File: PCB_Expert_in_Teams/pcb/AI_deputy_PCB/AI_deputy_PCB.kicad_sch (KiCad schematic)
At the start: 23 parts, among them J1 Piezo Electric, J3 Haptic Power and GND, J4 UART, J5 JST CONN from MCU, J6 JTAG, Q1 NMOS, SW1 BOOT SWITCH, SW2 RESET SWITCH, U2 ESP32-WROOM-32UE

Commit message: updating repo from desktop
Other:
- note added: "Keep as close to MCU pins as possible"
- note removed: "Keep close to MCU pins as possible"
- moved on the sheet: C1, C3, J1, J4, L1, Q1, R2, R3, R4, SW1A, SW2A

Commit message: progress on PCB + matlab calculations
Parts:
- added J15: Conn_01x04_Socket, symbol Connector:Conn_01x04_Socket
- J1: footprint Connector_JST:JST_XH_B1B-XH-AM_1x01_P2.50mm_Vertical -> Connector_JST:JST_XH_S2B-XH-A-1_1x02_P2.50mm_Horizontal
- Q1: footprint (none) -> Package_TO_SOT_SMD:TO-252-3_TabPin2
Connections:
- net +3V3: now also J15.2 (Pin_2)
- net GND: now also J15.1 (Pin_1)
- net Signal Left: now reaches U2.10 (IO25)
- net Signal Left: now also J15.3 (Pin_3)
- net Signal Right: now reaches U2.11 (IO26)
- net Signal Right: now also J15.4 (Pin_4)
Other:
- added sheet Stepdown3v3 (stepdown3v3.kicad_sch)
- added sheet stepup12v (stepup12v.kicad_sch)

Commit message: 29/10/update
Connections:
- net VDD is gone; now on net VDD33: C9.2
- net USB_TX: now reaches J4.3 (Pin_3), U2.34 (RXD0/IO3)
- net USB_RX: now reaches J4.2 (Pin_2), U2.35 (TXD0/IO1)
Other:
- sheet PD and UART renamed PD and USBC
- added sheet LI_Charge_IC (LI_Charge_IC.kicad_sch)
- added sheet UART (UART.kicad_sch)
- note added: "connect me"
- note added: "find fitting res value for led"
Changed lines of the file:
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@@
 	(title_block
 		(title "AI Deputy")
-		(date "2025-09-24")
+		(date "2025-10-29")
 		(rev "v0.1")
 		(company "Area 42 & Albers-Online Psykologi")
@@
 		)
 	)
+	(text "connect me\n"
+		(exclude_from_sim no)
+		(at 181.356 122.174 0)
+		(effects
+			(font
+				(size 1.27 1.27)
+			)
+		)
+	)
+	(text "find fitting res \nvalue for led\n"
+		(exclude_from_sim no)
+		(at 198.374 53.594 0)
+		(effects
+			(font
+				(size 1.27 1.27)
+			)
+		)
+	)
 	(text_box ""
 		(exclude_from_sim no)
@@
 		)
 	)
-	(global_label "VDD"
-		(shape input)
-		(at 161.29 60.96 270)
-		(fields_autoplaced yes)
-		(effects
-			(font
-				(size 1.27 1.27)
-			)
-			(justify right)
-		)
-		(property "Intersheetrefs" "${INTERSHEET_REFS}"
-			(at 161.29 67.5738 90)
-			(effects
-				(font
-					(size 1.27 1.27)
-				)
-				(justify right)
-				(hide yes)
-			)
-		)
-	)
 	(global_label "EN_ESP32"
 		(shape input)
@@
 		)
 	)
+	(global_label "USB_RX"
+		(shape input)
+		(at 185.42 92.71 90)
+		(fields_autoplaced yes)
+		(effects
+			(font
+				(size 1.27 1.27)
+			)
+			(justify left)
+		)
+		(property "Intersheetrefs" "${INTERSHEET_REFS}"
+			(at 185.42 82.4677 90)
+			(effects
+				(font
+					(size 1.27 1.27)
+				)
+				(justify left)
+				(hide yes)
+			)
+		)
+	)
 	(global_label "TDI"
 		(shape input)
@@
 		)
 	)
+	(global_label "PD_INT"
+		(shape input)
+		(at 177.8 125.73 0)
+		(fields_autoplaced yes)
+		(effects
+			(font
+				(size 1.27 1.27)
+			)
+			(justify left)
+		)
+		(property "Intersheetrefs" "${INTERSHEET_REFS}"
+			(at 187.1957 125.73 0)
+			(effects
+				(font
+					(size 1.27 1.27)
+				)
+				(justify left)
+				(hide yes)
+			)
+		)
+	)
+	(global_label "USB_TX"
+		(shape input)
+		(at 190.5 96.52 270)
+		(fields_autoplaced yes)
+		(effects
+			(font
+				(size 1.27 1.27)
+			)
+			(justify right)
+		)
+		(property "Intersheetrefs" "${INTERSHEET_REFS}"
+			(at 190.5 106.4599 90)
+			(effects
+				(font
+					(size 1.27 1.27)
+				)
+				(justify right)
+				(hide yes)
+			)
+		)
+	)
 	(global_label "TDI"
 		(shape input)
@@
 		)
 	)
+	(global_label "VDD33"
+		(shape input)
+		(at 161.29 60.96 270)
+		(fields_autoplaced yes)
+		(effects
+			(font
+				(size 1.27 1.27)
+			)
+			(justify right)
+		)
+		(property "Intersheetrefs" "${INTERSHEET_REFS}"
+			(at 161.29 69.9928 90)
+			(effects
+				(font
+					(size 1.27 1.27)
+				)
+				(justify right)
+				(hide yes)
+			)
+		)
+	)
 	(global_label "TMS"
 		(shape input)
@@
 			(color 0 0 0 0.0000)
 		)
-		(property "Sheetname" "PD and UART"
+		(property "Sheetname" "PD and USBC"
 			(at 231.14 22.1484 0)
 			(effects
@@
 	)
 	(sheet
+		(at 125.73 16.51)
+		(size 25.4 17.78)
+		(exclude_from_sim no)
+		(in_bom yes)
+		(on_board yes)
+		(dnp no)
+		(fields_autoplaced yes)
+		(stroke
+			(width 0.1524)
+			(type solid)
+		)
+		(fill
+			(color 0 0 0 0.0000)
+		)
+		(property "Sheetname" "UART"
+			(at 125.73 15.7984 0)
+			(effects
+				(font
+					(size 1.27 1.27)
+				)
+				(justify left bottom)
+			)
+		)
+		(property "Sheetfile" "UART.kicad_sch"
+			(at 125.73 34.8746 0)
+			(effects
+				(font
+					(size 1.27 1.27)
+				)
+				(justify left top)
+			)
+		)
+		(instances
+			(project "AI_deputy_PCB"
+				(path "/3784b751-4d5b-4452-8288-14e483e1cb48"
+					(page "7")
+				)
+			)
+		)
+	)
+	(sheet
 		(at 255.27 57.15)
 		(size 19.05 22.86)
@@
 				)
 			)
+		)
+	)
+	(sheet
+		(at 190.5 21.59)
+		(size 29.21 20.32)
+		(exclude_from_sim no)
+		(in_bom yes)
+		(on_board yes)
+		(dnp no)
+		(fields_autoplaced yes)
+		(stroke
+			(width 0.1524)
+			(type solid)
+		)
+		(fill
+			(color 0 0 0 0.0000)
+		)
+		(property "Sheetname" "LI_Charge_IC"
+			(at 190.5 20.8784 0)
+			(effects
+				(font
+					(size 1.27 1.27)
+				)
+				(justify left bottom)
+			)
+		)
+		(property "Sheetfile" "LI_Charge_IC.kicad_sch"
+			(at 190.5 42.4946 0)
+			(effects
+				(font
+					(size 1.27 1.27)
+				)
+				(justify left top)
+			)
+		)
+		(instances
+			(project "AI_deputy_PCB"
+				(path "/3784b751-4d5b-4452-8288-14e483e1cb48"
+					(page "8")
+				)
+			)

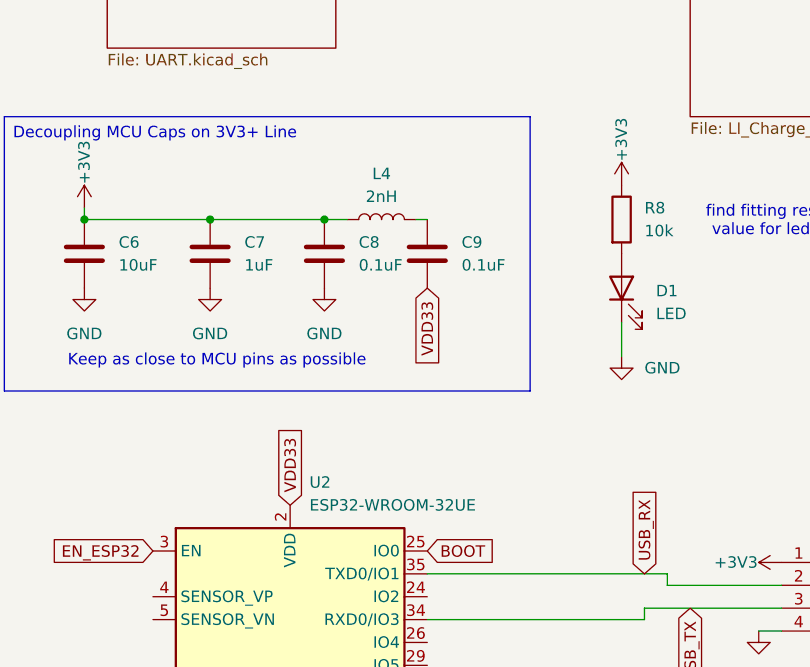
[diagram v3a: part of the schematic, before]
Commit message: update some schematic footprints
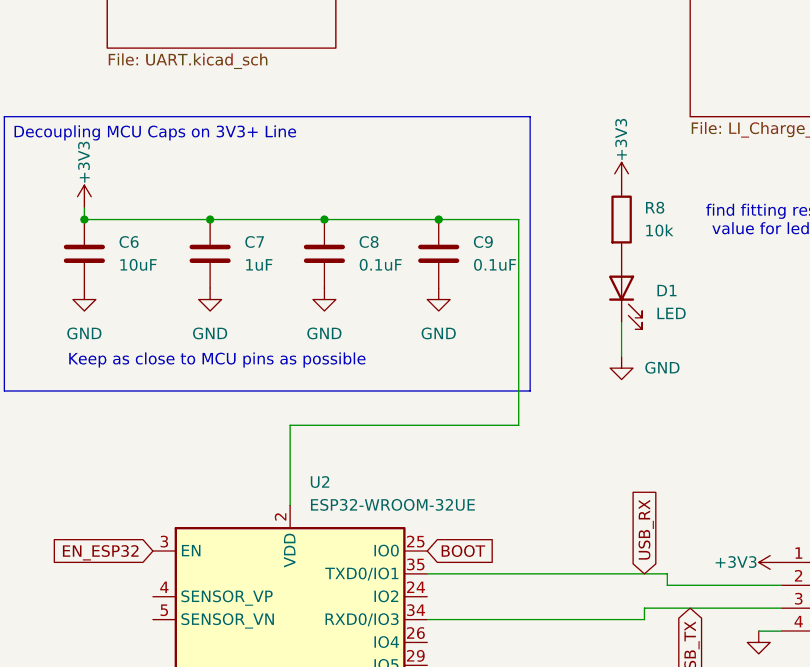
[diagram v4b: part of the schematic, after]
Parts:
- removed L4: 2nH, symbol Device:L
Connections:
- net VDD33 is gone; now on net +3V3: C9.2, U2.2 (VDD)
- net GND: now also C9.1
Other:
- moved on the sheet: C9
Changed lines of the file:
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@@
 	)
 	(junction
+		(at 162.56 53.34)
+		(diameter 0)
+		(color 0 0 0 0)
+	)
+	(junction
 		(at 82.55 180.34)
 		(diameter 0)
@@
 	(wire
 		(pts
+			(xy 171.45 76.2) (xy 146.05 76.2)
+		)
+		(stroke
+			(width 0)
+			(type default)
+		)
+	)
+	(wire
+		(pts
 			(xy 46.99 168.91) (xy 53.34 168.91)
 		)
@@
 	(wire
 		(pts
-			(xy 149.86 53.34) (xy 152.4 53.34)
+			(xy 149.86 53.34) (xy 162.56 53.34)
 		)
 		(stroke
@@
 	(wire
 		(pts
+			(xy 171.45 53.34) (xy 171.45 76.2)
+		)
+		(stroke
+			(width 0)
+			(type default)
+		)
+	)
+	(wire
+		(pts
 			(xy 161.29 97.79) (xy 185.42 97.79)
 		)
@@
 	(wire
 		(pts
+			(xy 146.05 76.2) (xy 146.05 85.09)
+		)
+		(stroke
+			(width 0)
+			(type default)
+		)
+	)
+	(wire
+		(pts
 			(xy 38.1 179.07) (xy 43.18 179.07)
 		)
@@
 	(wire
 		(pts
-			(xy 160.02 53.34) (xy 161.29 53.34)
+			(xy 162.56 53.34) (xy 171.45 53.34)
 		)
 		(stroke
@@
 		)
 	)
-	(global_label "VDD33"
-		(shape input)
-		(at 146.05 85.09 90)
-		(fields_autoplaced yes)
-		(effects
-			(font
-				(size 1.27 1.27)
-			)
-			(justify left)
-		)
-		(property "Intersheetrefs" "${INTERSHEET_REFS}"
-			(at 146.05 76.0572 90)
-			(effects
-				(font
-					(size 1.27 1.27)
-				)
-				(justify left)
-				(hide yes)
-			)
-		)
-	)
 	(global_label "SDA"
 		(shape input)
@@
 		)
 	)
-	(global_label "VDD33"
-		(shape input)
-		(at 161.29 60.96 270)
-		(fields_autoplaced yes)
-		(effects
-			(font
-				(size 1.27 1.27)
-			)
-			(justify right)
-		)
-		(property "Intersheetrefs" "${INTERSHEET_REFS}"
-			(at 161.29 69.9928 90)
-			(effects
-				(font
-					(size 1.27 1.27)
-				)
-				(justify right)
-				(hide yes)
-			)
-		)
-	)
 	(global_label "TMS"
 		(shape input)
@@
 	)
 	(symbol
+		(lib_id "power:GND")
+		(at 162.56 60.96 0)
+		(unit 1)
+		(exclude_from_sim no)
+		(in_bom yes)
+		(on_board yes)
+		(dnp no)
+		(fields_autoplaced yes)
+		(property "Reference" "#PWR0109"
+			(at 162.56 67.31 0)
+			(effects
+				(font
+					(size 1.27 1.27)
+				)
+				(hide yes)
+			)
+		)
+		(property "Value" "GND"
+			(at 162.56 66.04 0)
+			(effects
+				(font
+					(size 1.27 1.27)
+				)
+			)
+		)
+		(property "Footprint" ""
+			(at 162.56 60.96 0)
+			(effects
+				(font
+					(size 1.27 1.27)
+				)
+				(hide yes)
+			)
+		)
+		(property "Datasheet" ""
+			(at 162.56 60.96 0)
+			(effects
+				(font
+					(size 1.27 1.27)
+				)
+				(hide yes)
+			)
+		)
+		(property "Description" "Power symbol creates a global label with name \"GND\" , ground"
+			(at 162.56 60.96 0)
+			(effects
+				(font
+					(size 1.27 1.27)
+				)
+				(hide yes)
+			)
+		)
+		(pin "1"
+		)
+		(instances
+			(project "AI_deputy_PCB"
+				(path "/3784b751-4d5b-4452-8288-14e483e1cb48"
+					(reference "#PWR0109")
+					(unit 1)
+				)
+			)
+		)
+	)
+	(symbol
 		(lib_id "power:+3V3")
 		(at 251.46 132.08 90)
@@
 	(symbol
 		(lib_id "Device:C")
-		(at 161.29 57.15 0)
+		(at 162.56 57.15 180)
 		(unit 1)
 		(exclude_from_sim no)
@@
 		(fields_autoplaced yes)
 		(property "Reference" "C9"
-			(at 165.1 55.8799 0)
+			(at 166.37 55.8799 0)
 			(effects
 				(font
 					(size 1.27 1.27)
 				)
-				(justify left)
+				(justify right)
 			)
 		)
 		(property "Value" "0.1uF"
-			(at 165.1 58.4199 0)
+			(at 166.37 58.4199 0)
 			(effects
 				(font
 					(size 1.27 1.27)
 				)
-				(justify left)
+				(justify right)
 			)
 		)
 		(property "Footprint" "Capacitor_SMD:C_0805_2012Metric_Pad1.18x1.45mm_HandSolder"
-			(at 162.2552 60.96 0)
+			(at 161.5948 53.34 0)
 			(effects
 				(font
@@
 		)
 		(property "Datasheet" "~"
-			(at 161.29 57.15 0)
+			(at 162.56 57.15 0)
 			(effects
 				(font
@@
 		)
 		(property "Description" "Unpolarized capacitor"
-			(at 161.29 57.15 0)
+			(at 162.56 57.15 0)
 			(effects
 				(font
@@
 					(unit 1)
 				)
-			)
-		)
-	)
-	(symbol
-		(lib_id "Device:L")
-		(at 156.21 53.34 90)
-		(unit 1)
-		(exclude_from_sim no)
-		(in_bom yes)
-		(on_board yes)
-		(dnp no)
-		(fields_autoplaced yes)
-		(property "Reference" "L4"
-			(at 156.21 48.26 90)
-			(effects
-				(font
-					(size 1.27 1.27)
-				)
-			)
-		)
-		(property "Value" "2nH"
-			(at 156.21 50.8 90)
-			(effects
-				(font
-					(size 1.27 1.27)
-				)
-			)
-		)
-		(property "Footprint" ""
-			(at 156.21 53.34 0)
-			(effects
-				(font
-					(size 1.27 1.27)
-				)
-				(hide yes)
-			)
-		)
-		(property "Datasheet" "~"
-			(at 156.21 53.34 0)
-			(effects
-				(font
-					(size 1.27 1.27)
-				)
-				(hide yes)
-			)
-		)
-		(property "Description" "Inductor"
-			(at 156.21 53.34 0)
-			(effects
-				(font
-					(size 1.27 1.27)
-				)
-				(hide yes)
-			)
-		)
-		(pin "1"
-		)
-		(pin "2"
-		)
-		(instances
-			(project "AI_deputy_PCB"
-				(path "/3784b751-4d5b-4452-8288-14e483e1cb48"
-					(reference "L4")
-					(unit 1)
-				)

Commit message: update pcb from desktop
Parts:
- R2, R4: footprint (none) -> Resistor_SMD:R_0805_2012Metric_Pad1.20x1.40mm_HandSolder
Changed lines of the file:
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@@
 			)
 		)
-		(property "Footprint" ""
+		(property "Footprint" "Resistor_SMD:R_0805_2012Metric_Pad1.20x1.40mm_HandSolder"
 			(at 80.772 175.26 90)
 			(effects
@@
 			)
 		)
-		(property "Footprint" ""
+		(property "Footprint" "Resistor_SMD:R_0805_2012Metric_Pad1.20x1.40mm_HandSolder"
 			(at 32.512 129.54 90)
 			(effects

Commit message: update schematic from desktop
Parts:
- removed SW1: BOOT SWITCH, symbol Switch:SW_DPST_x2
- removed SW2: RESET SWITCH, symbol Switch:SW_DPST_x2
- added S1, S2: 430773034825, EXT_AI_DEPUTY_Library:430773034825, symbol Wurth Buttons:430773034825
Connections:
- net BOOT: now also S1.1, S1.2
- net EN_ESP32: now also C3.1, R2.2, S2.1, S2.2
- net GND: now also S1.3, S1.4, S2.3, S2.4
- net PD_INT: now also U2.31 (IO19)
- net DAC_LRCK: now reaches U2.27 (IO16)
- net DAC_DIN: now reaches U2.28 (IO17)
- net DAC_BCK: now reaches U2.30 (IO18)
- net MUTE: now reaches U2.37 (IO23)
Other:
- note removed: "connect me"
- moved on the sheet: R7

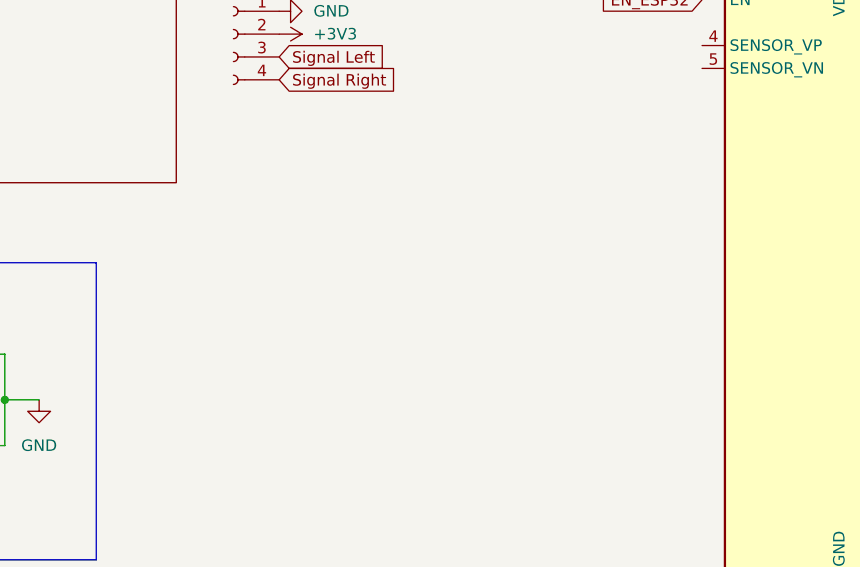
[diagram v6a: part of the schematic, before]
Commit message: pcb v0.1 plus cad render for mech students
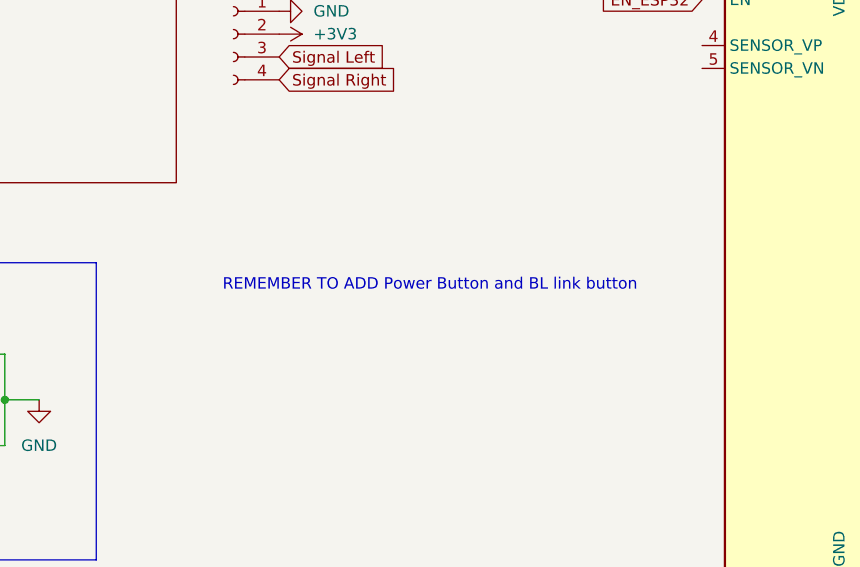
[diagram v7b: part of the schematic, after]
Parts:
- J15: footprint (none) -> Connector_JST:JST_XH_S4B-XH-A_1x04_P2.50mm_Horizontal
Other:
- note added: "REMEMBER TO ADD Power Button and BL link button"
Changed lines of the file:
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@@
+		)
+	)
+	(text "REMEMBER TO ADD Power Button and BL link button\n"
+		(exclude_from_sim no)
+		(at 100.584 121.92 0)
+		(effects
+			(font
+				(size 1.27 1.27)
+			)
 		)
 	)
@@
 			)
 		)
-		(property "Footprint" ""
+		(property "Footprint" "Connector_JST:JST_XH_S4B-XH-A_1x04_P2.50mm_Horizontal"
 			(at 78.74 93.98 0)
 			(effects
